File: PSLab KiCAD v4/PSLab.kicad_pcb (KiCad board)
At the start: 4 copper layers, 101.6 x 53.3 mm, 142 parts, among them CON1 USB-MICRO-B, J1 Programmer, J12 Sensors, J2 SQRs, J3 LA, J4 OSC_Pins, J5 Sin, J6 I2C, J7 IDs, J8 TX_RX_ES, J9 Test_Vs, P1 Power_Sources, P7 NRF, Q1 MMBT3906, Q2 MMBT3904, Q3 MMBT3906, U1 MCP2200, U10 TL082, U11 6S21, U12 6S21, U13 TL082, U15 ESP8266, U16 TL082, U2 74HC126, U3 PIC24EP256GP204, U4 TC1240A, U5 7660, U6 LM1117-3.3, U7 LM324, U8 TL082, U9 MCP4728, X1 12MHz

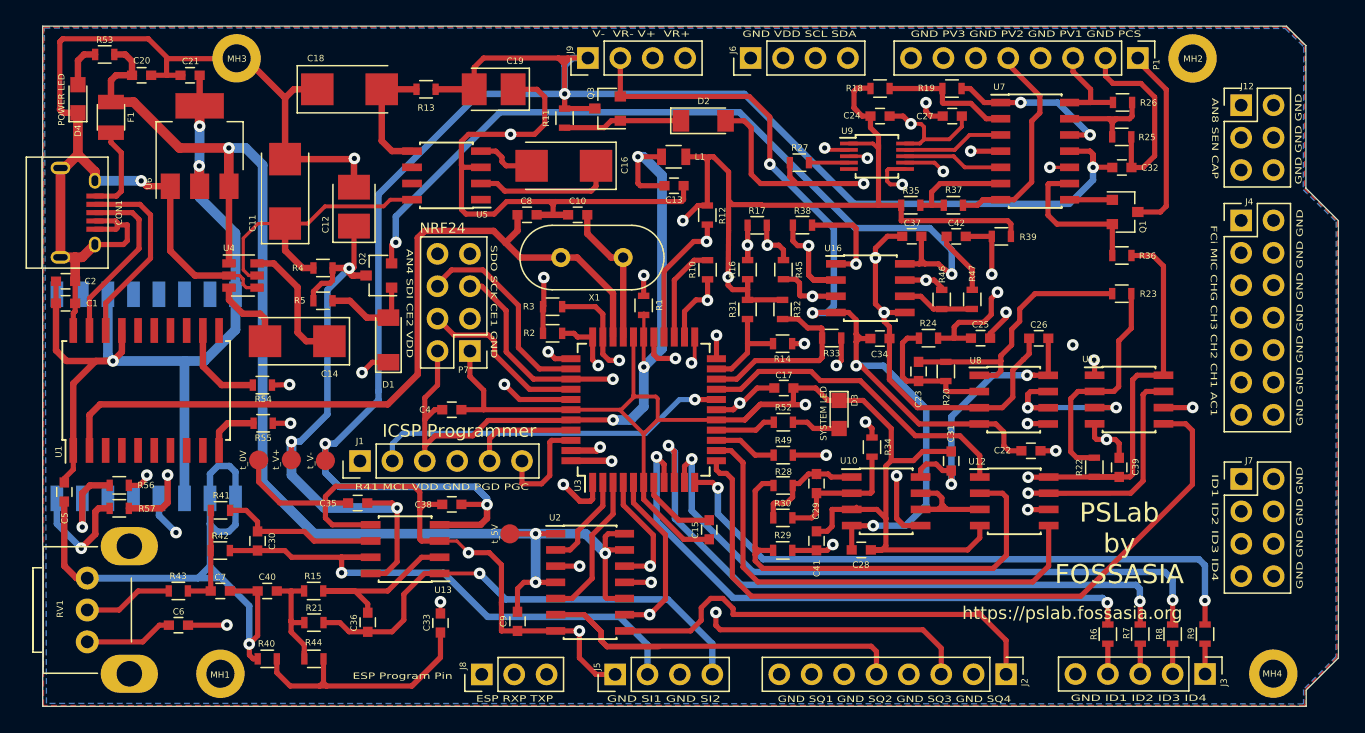
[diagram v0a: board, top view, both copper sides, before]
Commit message: Added breakouts for MCP2200 & PIC24 (#36)
* Added breakouts for MCP2200

* Added guard rings for OSC

* Grounded mount holes

* Gerber files updated
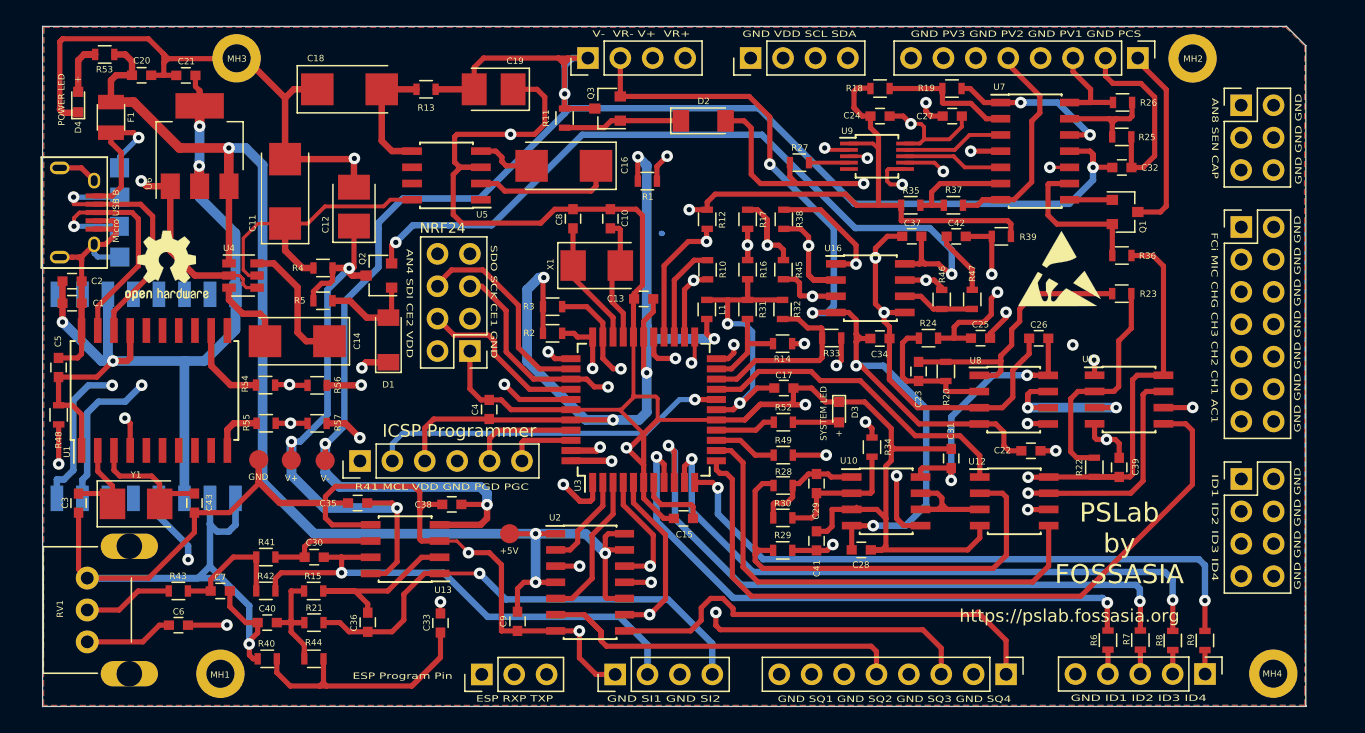
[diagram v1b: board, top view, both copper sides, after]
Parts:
- removed t_0V, t_5V, t_V+, t_V-: TEST, Measurement_Points:Measurement_Point_Round-SMD-Pad_Small
- added C3: 22p, Capacitors_SMD:C_0603, F.Cu at (93.8, 97.6)
- added C43: 22p, Capacitors_SMD:C_0603, F.Cu at (102.8, 97.6)
- added J10: GND, Measurement_Points:Measurement_Point_Square-SMD-Pad_Small, B.Cu at (97.0, 78.3)
- added J11: Vbus, Measurement_Points:Measurement_Point_Square-SMD-Pad_Small, B.Cu at (97.0, 71.4)
- added J13: D+, Measurement_Points:Measurement_Point_Square-SMD-Pad_Small, B.Cu at (97.0, 75.9)
- added J14: D-, Measurement_Points:Measurement_Point_Square-SMD-Pad_Small, B.Cu at (97.0, 73.7)
- added R48: 4.7k, Resistors_SMD:R_0603, F.Cu at (92.2, 90.7)
- added REF***: OSHW-Logo2_7.3x6mm_SilkScreen, Symbols:OSHW-Logo2_7.3x6mm_SilkScreen, F.Cu at (100.7, 79.0)
- added REF***: ESD-Logo_6.6x6mm_SilkScreen, Symbols:ESD-Logo_6.6x6mm_SilkScreen, F.Cu at (170.7, 79.2)
- added TP1: TEST, Measurement_Points:Measurement_Point_Round-SMD-Pad_Small, F.Cu at (113.1, 94.3)
- added TP2: TEST, Measurement_Points:Measurement_Point_Round-SMD-Pad_Small, F.Cu at (110.4, 94.3)
- added TP3: TEST, Measurement_Points:Measurement_Point_Round-SMD-Pad_Small, F.Cu at (127.5, 100.0)
- added TP4: TEST, Measurement_Points:Measurement_Point_Round-SMD-Pad_Small, F.Cu at (107.9, 94.2)
- added Y1: 12MHz, Crystals:Crystal_SMD_5032-2pin_5.0x3.2mm, F.Cu at (98.3, 97.7)
- CON1: value USB-MICRO-B -> USB-MINI-B
- D3, D4: footprint LEDs:LED_0805 -> LEDs:LED_0603
- L1: footprint Inductors_SMD:L_0805 -> Inductors_SMD:L_0603
- X1: value 12MHz -> 8MHz; footprint Crystals:Crystal_HC49-U_Vertical -> Crystals:Crystal_SMD_5032-2pin_5.0x3.2mm
- moved R56 17.4 mm to (112.5, 88.4), turned to 180 degrees
- moved R57 16.9 mm to (112.5, 91.4), turned to 180 degrees
- moved L1 12.2 mm to (143.0, 82.5), turned to 270 degrees
- moved C5 9.77 mm to (92.2, 87.0), turned to 90 degrees
- moved R1 9.74 mm to (138.3, 72.4), turned to 0 degrees
- moved C13 9.18 mm to (138.1, 81.6), turned to 0 degrees
- moved R41 5.10 mm to (108.4, 101.9)
- moved R42 4.77 mm to (108.4, 104.5)
- moved C30 4.62 mm to (112.2, 101.9), turned to 180 degrees
- moved C8 3.61 mm to (132.5, 75.3), turned to 270 degrees
- moved C4 2.93 mm to (126.0, 90.3), turned to 90 degrees
- moved X1 2.88 mm to (134.4, 79.0)
- moved C10 2.58 mm to (135.4, 75.3), turned to 270 degrees
- moved C40 2.48 mm to (108.5, 107.0)
- moved C15 2.21 mm to (141.2, 98.8), turned to 180 degrees
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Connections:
- C8 pad 2: 12MHz -> Net-(C8-Pad2)
- MH1 pad 1: (no net) -> GND
- MH4 pad 1: (no net) -> GND
- U1 pad 2: 12MHz -> OS1
- U1 pad 3: (no net) -> OS2
- U1 pad 4: (no net) -> Net-(R48-Pad2)
- U3 pad 31: 12MHz -> Net-(C8-Pad2)
- X1 pad 1: 12MHz -> Net-(C8-Pad2)
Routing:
- net 12MHz: track 68.6 -> 0.00 mm
- net /RxD: track 153.9 -> 94.4 mm, vias 3 -> 2
- net /TxD: track 124.1 -> 73.6 mm, vias 3 -> 2
- net GND: track 818.2 -> 851.2 mm, vias 15 -> 16
- net Vdd: track 239.2 -> 211.8 mm, vias 7 -> 9
- net V-: track 193.7 -> 168.2 mm
- net /ETxD: track 12.0 -> 37.2 mm, vias 1 -> 2
- net /ERxD: track 10.4 -> 33.3 mm, vias 1 -> 2
- net SINE1: track 68.5 -> 48.7 mm
- net +5V: track 123.3 -> 105.2 mm
- net SDO: track 83.7 -> 100.2 mm
- net AVdd: track 170.3 -> 154.7 mm
- net VR-: track 102.9 -> 87.8 mm
- net /SQR2: track 45.4 -> 31.2 mm
- net MCLR: track 42.9 -> 55.5 mm
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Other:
- board size 101.6 x 53.3 mm -> 99 x 53.3 mm
- rule via_min_size: 0.5 -> 0.3
- board text added: "+"
- board text added: "+5V"
- board text added: "4th Rev @ 29 Jan 18"
- board text added: "D+"
- board text added: "D-"
- board text added: "GND"
- board text added: "Micro USB B"
- board text added: "V+"
- board text added: "V-"
- board text added: "Vbus"
- board text removed: "4th Rev @ 23 Jan 17"
